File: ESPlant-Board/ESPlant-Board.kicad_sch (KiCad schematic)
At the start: 38 parts, among them J1 Conn_01x05, U1 HC-TYPE-C-16P-01A-G, U13 ESP32-C6-MINI-1/U, U3 Reset, U4 Boot, U5 Temp/Humid-Sensor, U6 Light sensor, U7 AMS1117-3_3, U8 MK-12C02-G025

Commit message: Board: Change from aht21 to aht21, fix kikit, produce board
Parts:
- U10, U11, U12, U2: footprint PCM_kikit:Tab_5mm -> CustomFootprints:MouseBites5mm
- U5: LCSC C2827328 -> C2757850; MPN C2827328 -> C2757850
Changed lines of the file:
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@@
       (effects (font (size 1.27 1.27)))
     )
-    (property "Footprint" "PCM_kikit:Tab_5mm" (at 255.27 160.02 0)
+    (property "Footprint" "CustomFootprints:MouseBites5mm" (at 255.27 160.02 0)
       (effects (font (size 1.27 1.27)) hide)
     )
@@
       (effects (font (size 1.27 1.27)))
     )
-    (property "Footprint" "PCM_kikit:Tab_5mm" (at 243.84 160.02 0)
+    (property "Footprint" "CustomFootprints:MouseBites5mm" (at 243.84 160.02 0)
       (effects (font (size 1.27 1.27)) hide)
     )
@@
       (effects (font (size 1.27 1.27)))
     )
-    (property "Footprint" "PCM_kikit:Tab_5mm" (at 219.71 160.02 0)
+    (property "Footprint" "CustomFootprints:MouseBites5mm" (at 219.71 160.02 0)
       (effects (font (size 1.27 1.27)) hide)
     )
@@
       (effects (font (size 1.27 1.27)) (justify left) hide)
     )
-    (property "LCSC" "C2827328" (at 33.02 91.44 0)
-      (effects (font (size 1.27 1.27)) hide)
-    )
-    (property "MPN" "C2827328" (at 33.02 91.44 0)
+    (property "LCSC" "C2757850" (at 33.02 91.44 0)
+      (effects (font (size 1.27 1.27)) hide)
+    )
+    (property "MPN" "C2757850" (at 33.02 91.44 0)
       (effects (font (size 1.27 1.27)) hide)
     )
@@
       (effects (font (size 1.27 1.27)))
     )
-    (property "Footprint" "PCM_kikit:Tab_5mm" (at 231.14 160.02 0)
-      (effects (font (size 1.27 1.27)) hide)
-    )
+    (property "Footprint" "CustomFootprints:MouseBites5mm" (at 231.14 160.02 0)
+      (effects (font (size 1.27 1.27)) hide)
+    )

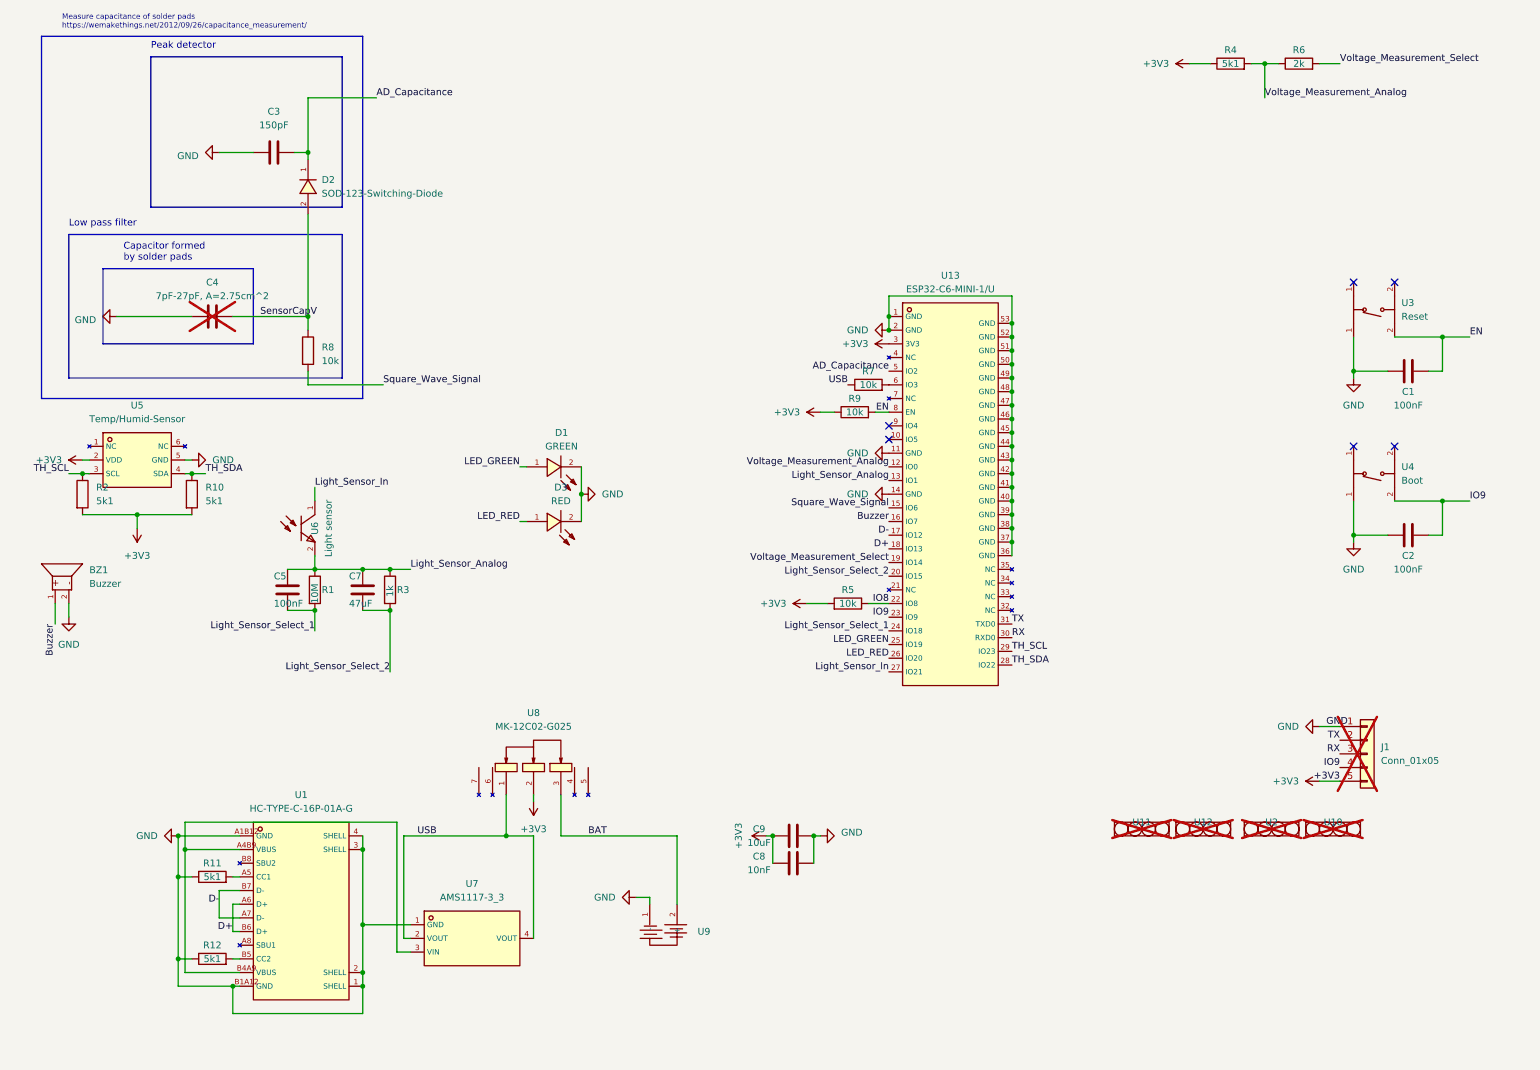
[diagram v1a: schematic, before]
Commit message: Board: Make ESPlant-Board 4 layer (wip)
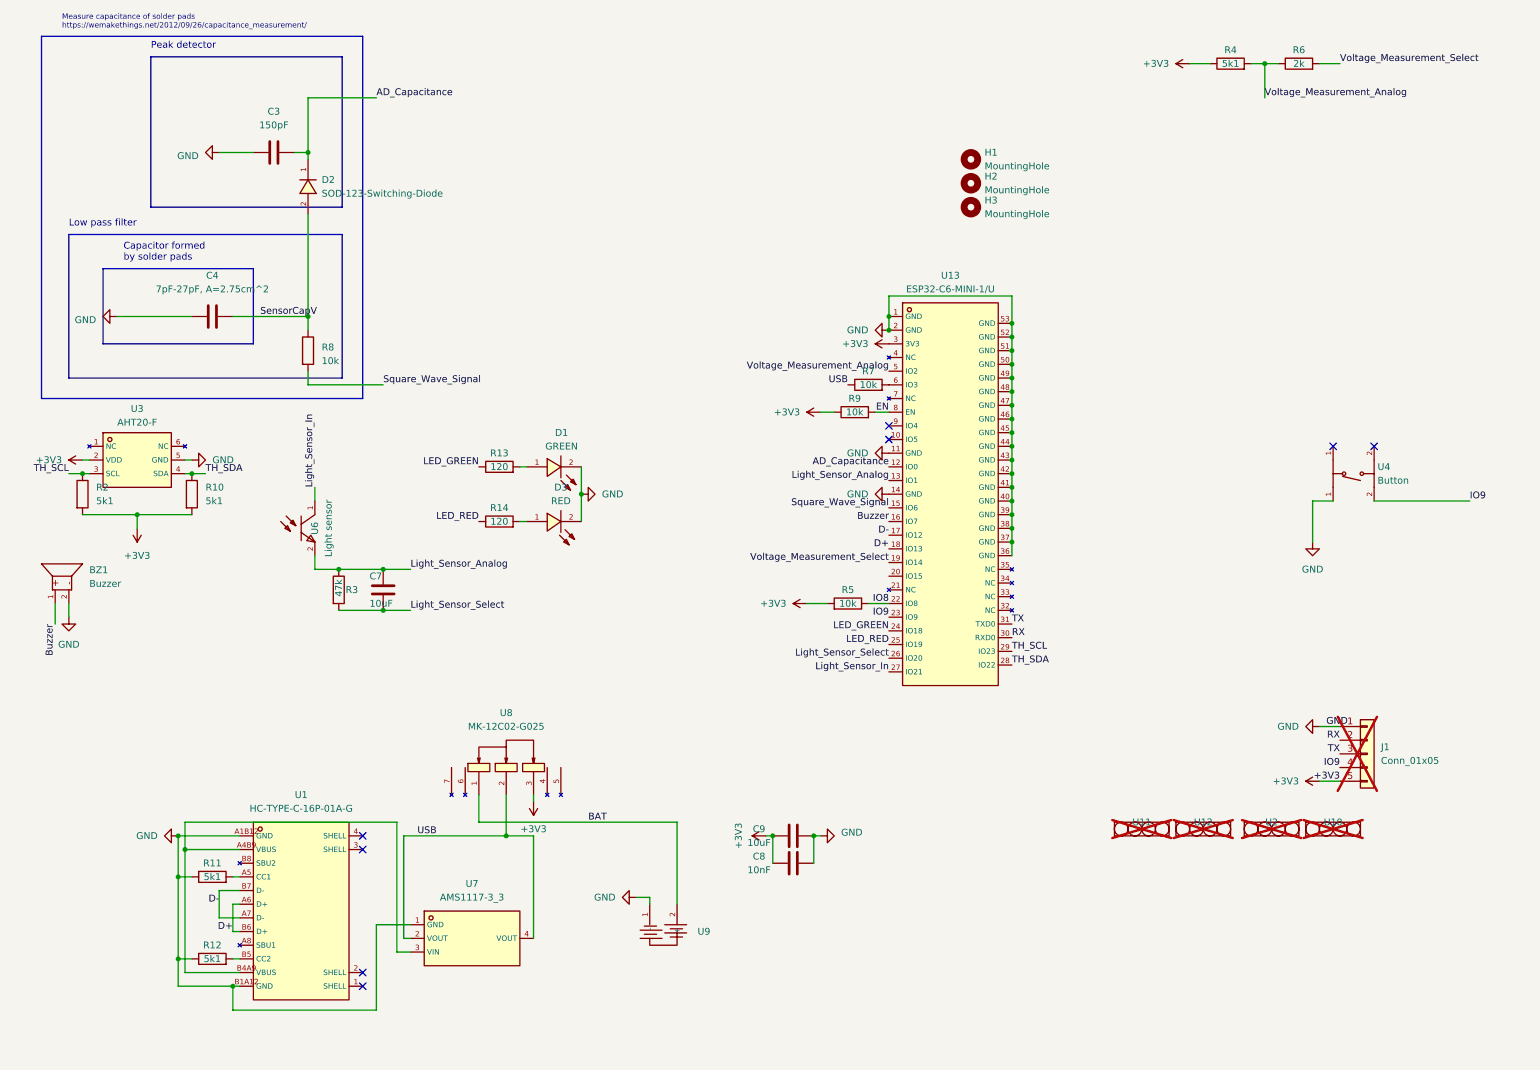
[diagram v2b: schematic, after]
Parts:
- removed C1, C2, C5: 100nF, Capacitor_SMD:C_0402_1005Metric, symbol Device:C
- removed R1: 10M, Resistor_SMD:R_0402_1005Metric, symbol Device:R
- removed U3: Reset, CustomFootprints:SW-SMD_4P-L5.1-W5.1-P3.70-LS6.5-TL-2, symbol Custom_Parts:Button
- removed U5: Temp/Humid-Sensor, CustomFootprints:SENSOR-SMD_L3.0-W3.0-P1.00-BR, symbol Custom_Parts:AHT21
- added H1, H2, H3: MountingHole, MountingHole:MountingHole_3.2mm_M3, symbol Mechanical:MountingHole
- added R13, R14: 120, Resistor_SMD:R_0402_1005Metric, symbol Device:R
- added U3: AHT20-F, CustomFootprints:SENSOR-SMD-6_AHT20, symbol Custom_Parts:AHT20-F
- C4: footprint (none) -> CustomFootprints:Sensor-Tip; now fitted
- C7: value 47uF -> 10uF; footprint Capacitor_SMD:C_0805_2012Metric -> Capacitor_SMD:C_0402_1005Metric; LCSC C16780 -> C15525; MPN C16780 -> C15525
- J1: footprint Connector_PinHeader_2.54mm:PinHeader_1x05_P2.54mm_Vertical -> CustomFootprints:PinHeader_1x05_P2.54mm_Vertical_SMD
- R3: value 1k -> 47k; LCSC C11702 -> C25792; MPN C11702 -> C25792
- U1: MPN (none) -> C2997435
- U4: value Boot -> Button; MPN C318884 -> (none)
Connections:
- net Light_Sensor_Select_1 is gone; now on net LED_GREEN: U13.24 (IO18)
- net +3V3: now also U8.3, U3.2 (VDD); no longer U8.2
- net AD_Capacitance: now also U13.12 (IO0); no longer U13.5 (IO2)
- net BAT: now also U8.1; no longer U8.3
- net GND: now also C4.2, U3.5 (GND); no longer C4.1, U1.1 (SHELL), U1.2 (SHELL), U1.3 (SHELL), U1.4 (SHELL)
- net LED_GREEN: now also R13.1; no longer D1.1 (A), U13.25 (IO19)
- net LED_RED: now also U13.25 (IO19), R14.1; no longer D3.1 (+), U13.26 (IO20)
- net RX: now also J1.2 (Pin_2); no longer J1.3 (Pin_3)
- net SensorCapV: now also C4.1; no longer C4.2
- net TH_SCL: now also U3.3 (SCL)
- net TH_SDA: now also U3.4 (SDA)
- net TX: now also J1.3 (Pin_3); no longer J1.2 (Pin_2)
- net USB: now also U8.2; no longer U8.1
- net Voltage_Measurement_Analog: now also U13.5 (IO2); no longer U13.12 (IO0)
- net Light_Sensor_Select_2 renamed Light_Sensor_Select
- net Light_Sensor_Select: now also U13.26 (IO20); no longer U13.20 (IO15)
- new net: D1.1 (A), R13.2
- new net: D3.1 (+), R14.2
- no-connect marks 6 -> 8
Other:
- moved on the sheet: C7, R3, U8

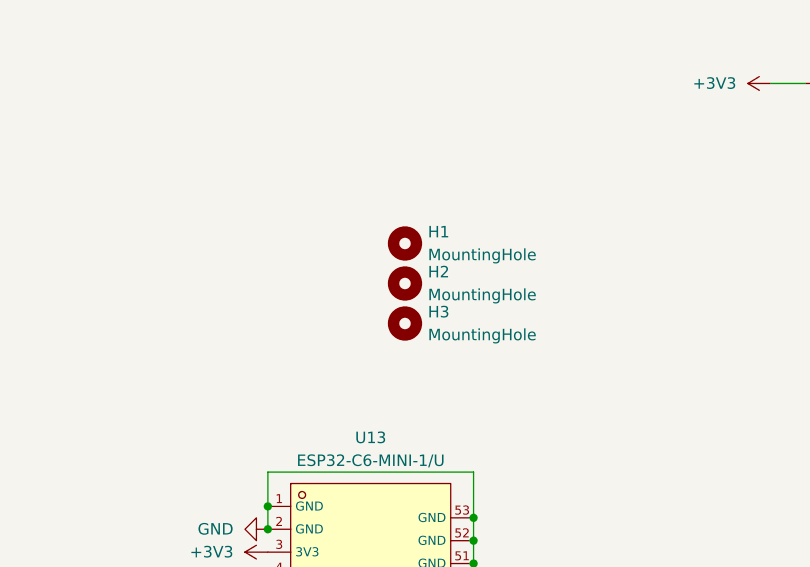
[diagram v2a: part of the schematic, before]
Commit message: Panel: Add panelization script
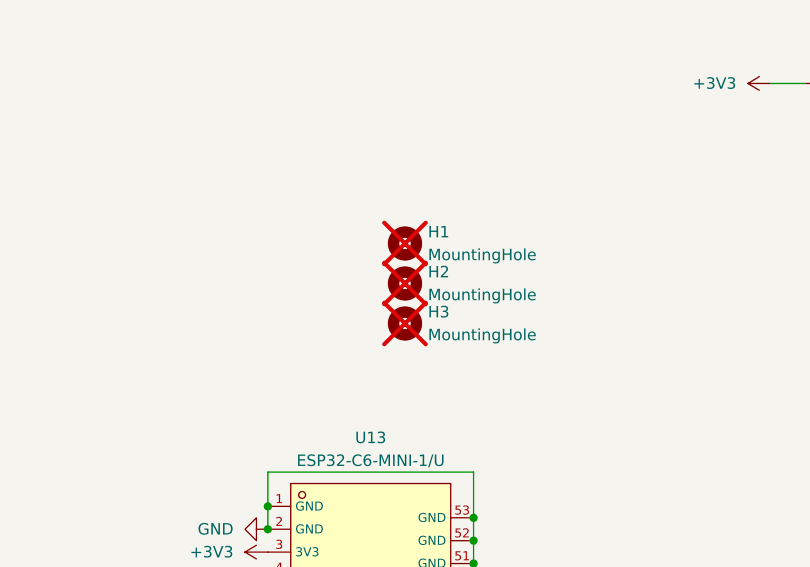
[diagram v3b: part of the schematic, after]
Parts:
- C4, J1, U9: LCSC / -> (none)
- H1, H2, H3: LCSC / -> (none); now not fitted; now left out of the parts list
- U10, U11, U12, U2: MPN (none) -> /
- U4: MPN (none) -> C318884
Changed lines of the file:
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@@
+      (effects (font (size 1.27 1.27)) hide)
+    )
+    (property "MPN" "/" (at 255.27 160.02 0)
       (effects (font (size 1.27 1.27)) hide)
     )
@@
       (effects (font (size 1.27 1.27)) hide)
     )
+    (property "MPN" "C318884" (at 257.81 93.98 0)
+      (effects (font (size 1.27 1.27)) hide)
+    )
     (pin "2")
     (pin "2")
@@
   )
   (symbol (lib_id "Mechanical:MountingHole") (at 187.96 35.56 0) (unit 1)
-    (in_bom yes) (on_board yes) (dnp no) (fields_autoplaced)
+    (in_bom no) (on_board yes) (dnp yes) (fields_autoplaced)
     (property "Reference" "H1" (at 190.5 34.29 0)
       (effects (font (size 1.27 1.27)) (justify left))
@@
       (effects (font (size 1.27 1.27)) hide)
     )
-    (property "LCSC" "/" (at 187.96 35.56 0)
+    (property "LCSC" "" (at 187.96 35.56 0)
       (effects (font (size 1.27 1.27)) hide)
     )
@@
       (effects (font (size 1.27 1.27)) hide)
     )
+    (property "MPN" "/" (at 243.84 160.02 0)
+      (effects (font (size 1.27 1.27)) hide)
+    )
     (instances
       (project "ESPlant-Board"
@@
   )
   (symbol (lib_id "Mechanical:MountingHole") (at 187.96 44.45 0) (unit 1)
-    (in_bom yes) (on_board yes) (dnp no) (fields_autoplaced)
+    (in_bom no) (on_board yes) (dnp yes) (fields_autoplaced)
     (property "Reference" "H3" (at 190.5 43.18 0)
       (effects (font (size 1.27 1.27)) (justify left))
@@
       (effects (font (size 1.27 1.27)) hide)
     )
-    (property "LCSC" "/" (at 187.96 44.45 0)
+    (property "LCSC" "" (at 187.96 44.45 0)
       (effects (font (size 1.27 1.27)) hide)
     )
@@
   )
   (symbol (lib_id "Mechanical:MountingHole") (at 187.96 40.005 0) (unit 1)
-    (in_bom yes) (on_board yes) (dnp no) (fields_autoplaced)
+    (in_bom no) (on_board yes) (dnp yes) (fields_autoplaced)
     (property "Reference" "H2" (at 190.5 38.735 0)
       (effects (font (size 1.27 1.27)) (justify left))
@@
       (effects (font (size 1.27 1.27)) hide)
     )
-    (property "LCSC" "/" (at 187.96 40.005 0)
+    (property "LCSC" "" (at 187.96 40.005 0)
       (effects (font (size 1.27 1.27)) hide)
     )
@@
     )
     (property "Datasheet" "" (at 219.71 160.02 0)
+      (effects (font (size 1.27 1.27)) hide)
+    )
+    (property "MPN" "/" (at 219.71 160.02 0)
       (effects (font (size 1.27 1.27)) hide)
     )
@@
       (effects (font (size 1.27 1.27)) hide)
     )
-    (property "LCSC" "/" (at 46.99 64.77 0)
+    (property "LCSC" "" (at 46.99 64.77 0)
       (effects (font (size 1.27 1.27)) hide)
     )
@@
       (effects (font (size 1.27 1.27)) hide)
     )
-    (property "LCSC" "/" (at 261.62 146.05 0)
+    (property "LCSC" "" (at 261.62 146.05 0)
       (effects (font (size 1.27 1.27)) hide)
     )
@@
       (effects (font (size 1.27 1.27)) hide)
     )
+    (property "MPN" "/" (at 231.14 160.02 0)
+      (effects (font (size 1.27 1.27)) hide)
+    )
     (instances
       (project "ESPlant-Board"
@@
       (effects (font (size 1.27 1.27)) hide)
     )
-    (property "LCSC" "/" (at 130.81 177.8 0)
-      (effects (font (size 1.27 1.27)) hide)
-    )
+    (property "LCSC" "" (at 130.81 177.8 0)
+      (effects (font (size 1.27 1.27)) hide)
+    )

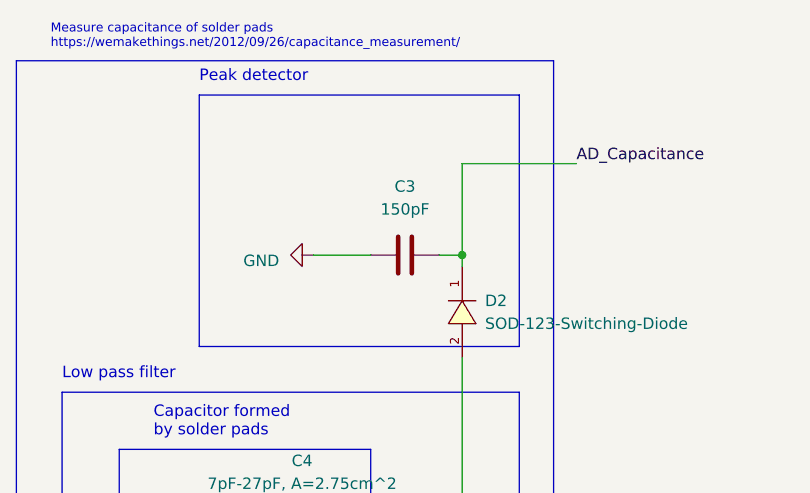
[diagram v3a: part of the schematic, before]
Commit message: Update capacitor size
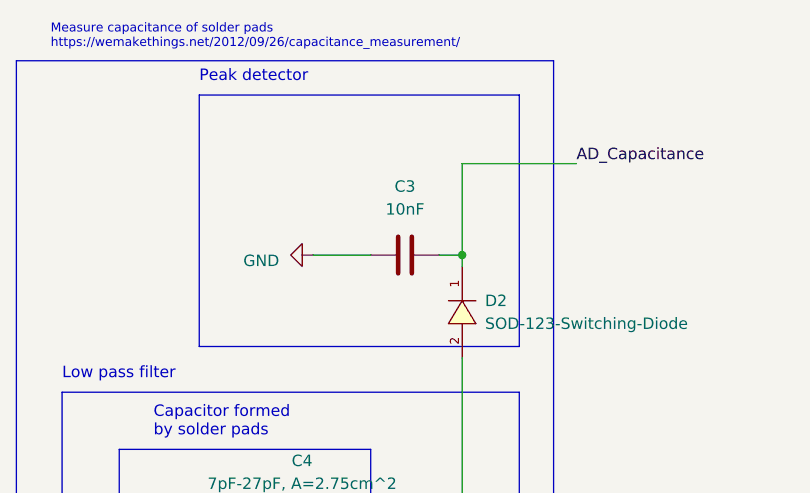
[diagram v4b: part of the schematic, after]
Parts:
- C3: value 150pF -> 10nF; LCSC C1527 -> C15195; MPN C1527 -> C15195
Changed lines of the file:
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@@
       (effects (font (size 1.27 1.27)))
     )
-    (property "Value" "150pF" (at 58.42 29.21 90)
+    (property "Value" "10nF" (at 58.42 29.21 90)
       (effects (font (size 1.27 1.27)))
     )
@@
       (effects (font (size 1.27 1.27)) hide)
     )
-    (property "LCSC" "C1527" (at 58.42 34.29 0)
+    (property "LCSC" "C15195" (at 58.42 34.29 0)
       (effects (font (size 1.27 1.27)) hide)
     )
-    (property "MPN" "C1527" (at 58.42 34.29 0)
+    (property "MPN" "C15195" (at 58.42 34.29 0)
       (effects (font (size 1.27 1.27)) hide)
     )
